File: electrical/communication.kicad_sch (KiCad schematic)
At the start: 13 parts

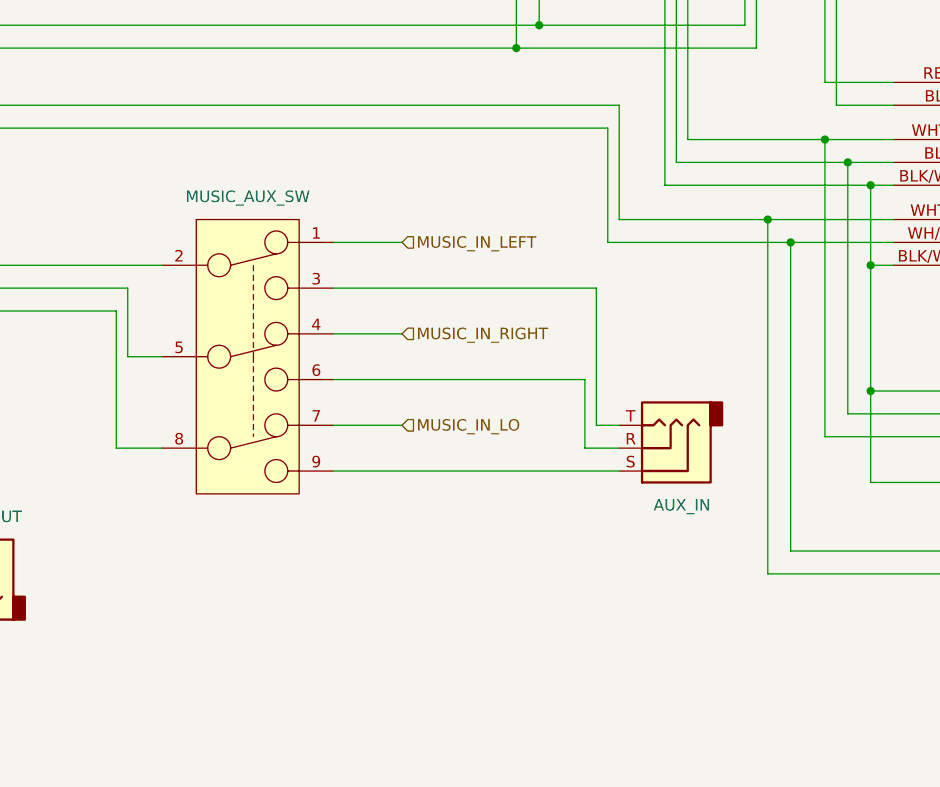
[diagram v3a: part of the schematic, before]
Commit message: Updated electrical to not use IBBS. Also, added BT adapter and 3P3T switch.
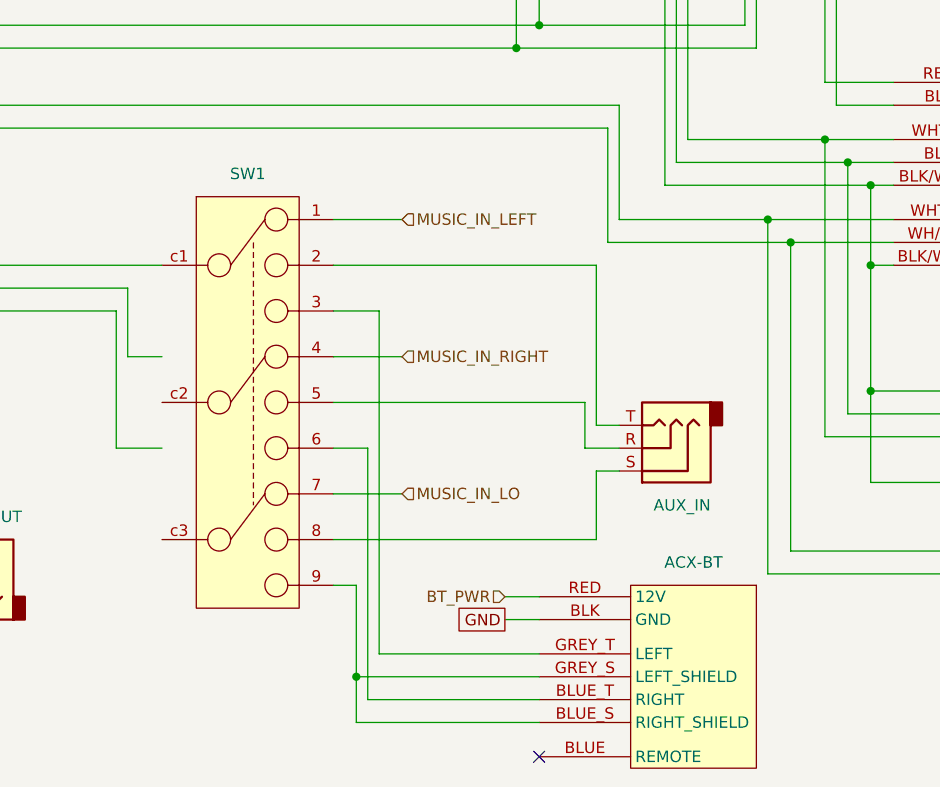
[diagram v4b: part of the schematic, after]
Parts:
- removed MUSIC_AUX_SW: ~, symbol flyerx:SW_3PDT_Toggle
- added ACX-BT: ~, symbol flyerx:AudioControl_ACX-BT1
- added SW1: ~, symbol flyerx:SW_3P3T
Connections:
- net GND: now also ACX-BT.BLK (GND)
- net MUSIC_IN_LEFT: now also SW1.1
- net MUSIC_IN_LO: now also SW1.7
- net MUSIC_IN_RIGHT: now also SW1.4
- net at AUX_IN.R: now also SW1.5
- net at AUX_IN.S: now also SW1.8
- net at AUX_IN.T: now also SW1.2
- net at GTR20.P2001_19 (MUSIC_IN_LEFT): now also SW1.c1
- new net: ACX-BT.GREY_T (LEFT), SW1.3
- new net: ACX-BT.BLUE_T (RIGHT), SW1.6
- new net: ACX-BT.BLUE_S (RIGHT_SHIELD), ACX-BT.GREY_S (LEFT_SHIELD), SW1.9
- new net BT_PWR: ACX-BT.RED (12V)
- no-connect marks 0 -> 1
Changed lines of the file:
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@@
   (junction (at 185.42 73.66) (diameter 0) (color 0 0 0 0)
   )
+  (junction (at 160.02 161.29) (diameter 0) (color 0 0 0 0)
+  )
   (junction (at 81.28 44.45) (diameter 0) (color 0 0 0 0)
   )
@@
   (junction (at 205.74 110.49) (diameter 0) (color 0 0 0 0)
   )
+  (no_connect (at 180.34 170.18))
   (wire (pts (xy 229.87 25.4) (xy 228.6 25.4))
     (stroke (width 0) (type default))
@@
     (stroke (width 0) (type default))
   )
+  (wire (pts (xy 176.53 152.4) (xy 180.34 152.4))
+    (stroke (width 0) (type default))
+  )
   (wire (pts (xy 106.68 124.46) (xy 106.68 151.13))
     (stroke (width 0) (type default))
@@
     (stroke (width 0) (type default))
   )
+  (wire (pts (xy 180.34 166.37) (xy 160.02 166.37))
+    (stroke (width 0) (type default))
+  )
   (wire (pts (xy 185.42 41.91) (xy 185.42 73.66))
     (stroke (width 0) (type default))
@@
     (stroke (width 0) (type default))
   )
-  (wire (pts (xy 157.48 118.11) (xy 186.69 118.11))
+  (wire (pts (xy 157.48 115.57) (xy 186.69 115.57))
     (stroke (width 0) (type default))
   )
@@
     (stroke (width 0) (type default))
   )
+  (wire (pts (xy 176.53 154.94) (xy 180.34 154.94))
+    (stroke (width 0) (type default))
+  )
   (wire (pts (xy 217.17 73.66) (xy 219.71 73.66))
     (stroke (width 0) (type default))
@@
     (stroke (width 0) (type default))
   )
+  (wire (pts (xy 161.29 135.89) (xy 157.48 135.89))
+    (stroke (width 0) (type default))
+  )
   (wire (pts (xy 73.66 80.01) (xy 195.58 80.01))
     (stroke (width 0) (type default))
@@
     (stroke (width 0) (type default))
   )
+  (wire (pts (xy 186.69 138.43) (xy 189.23 138.43))
+    (stroke (width 0) (type default))
+  )
   (wire (pts (xy 134.62 125.73) (xy 138.43 125.73))
     (stroke (width 0) (type default))
@@
     (stroke (width 0) (type default))
   )
+  (wire (pts (xy 160.02 161.29) (xy 160.02 151.13))
+    (stroke (width 0) (type default))
+  )
   (wire (pts (xy 204.47 80.01) (xy 219.71 80.01))
     (stroke (width 0) (type default))
@@
     (stroke (width 0) (type default))
   )
-  (wire (pts (xy 157.48 113.03) (xy 165.1 113.03))
+  (wire (pts (xy 186.69 146.05) (xy 186.69 138.43))
+    (stroke (width 0) (type default))
+  )
+  (wire (pts (xy 157.48 110.49) (xy 165.1 110.49))
     (stroke (width 0) (type default))
   )
@@
     (stroke (width 0) (type default))
   )
+  (wire (pts (xy 180.34 163.83) (xy 161.29 163.83))
+    (stroke (width 0) (type default))
+  )
   (wire (pts (xy 234.95 52.07) (xy 217.17 52.07))
     (stroke (width 0) (type default))
@@
     (stroke (width 0) (type default))
   )
+  (wire (pts (xy 160.02 161.29) (xy 160.02 166.37))
+    (stroke (width 0) (type default))
+  )
   (wire (pts (xy 73.66 73.66) (xy 185.42 73.66))
     (stroke (width 0) (type default))
@@
     (stroke (width 0) (type default))
   )
-  (wire (pts (xy 186.69 118.11) (xy 186.69 133.35))
+  (wire (pts (xy 186.69 115.57) (xy 186.69 133.35))
     (stroke (width 0) (type default))
   )
@@
     (stroke (width 0) (type default))
   )
-  (wire (pts (xy 157.48 123.19) (xy 165.1 123.19))
+  (wire (pts (xy 157.48 125.73) (xy 165.1 125.73))
     (stroke (width 0) (type default))
   )
@@
     (stroke (width 0) (type default))
   )
+  (wire (pts (xy 161.29 163.83) (xy 161.29 135.89))
+    (stroke (width 0) (type default))
+  )
   (wire (pts (xy 73.66 97.79) (xy 189.23 97.79))
     (stroke (width 0) (type default))
@@
     (stroke (width 0) (type default))
   )
-  (wire (pts (xy 185.42 128.27) (xy 185.42 135.89))
+  (wire (pts (xy 185.42 130.81) (xy 185.42 135.89))
     (stroke (width 0) (type default))
   )
@@
     (stroke (width 0) (type default))
   )
-  (wire (pts (xy 157.48 128.27) (xy 185.42 128.27))
+  (wire (pts (xy 160.02 161.29) (xy 180.34 161.29))
+    (stroke (width 0) (type default))
+  )
+  (wire (pts (xy 157.48 130.81) (xy 185.42 130.81))
     (stroke (width 0) (type default))
   )
@@
     (stroke (width 0) (type default))
   )
-  (wire (pts (xy 157.48 138.43) (xy 189.23 138.43))
+  (wire (pts (xy 157.48 146.05) (xy 186.69 146.05))
     (stroke (width 0) (type default))
   )
@@
     (stroke (width 0) (type default))
   )
-  (wire (pts (xy 157.48 133.35) (xy 165.1 133.35))
+  (wire (pts (xy 157.48 140.97) (xy 165.1 140.97))
     (stroke (width 0) (type default))
   )
@@
     (stroke (width 0) (type default))
   )
+  (wire (pts (xy 180.34 158.75) (xy 162.56 158.75))
+    (stroke (width 0) (type default))
+  )
   (wire (pts (xy 73.66 118.11) (xy 134.62 118.11))
     (stroke (width 0) (type default))
   )
+  (wire (pts (xy 162.56 158.75) (xy 162.56 120.65))
+    (stroke (width 0) (type default))
+  )
   (wire (pts (xy 73.66 77.47) (xy 196.85 77.47))
     (stroke (width 0) (type default))
@@
   )
   (wire (pts (xy 229.87 132.08) (xy 214.63 132.08))
+    (stroke (width 0) (type default))
+  )
+  (wire (pts (xy 162.56 120.65) (xy 157.48 120.65))
+    (stroke (width 0) (type default))
+  )
+  (wire (pts (xy 160.02 151.13) (xy 157.48 151.13))
     (stroke (width 0) (type default))
   )
@@
     (property "Intersheetrefs" "${INTERSHEET_REFS}" (at 60.3544 151.13 0)
       (effects (font (size 1.27 1.27)) (justify left) hide)
+    )
+  )
+  (global_label "GND" (shape passive) (at 176.53 154.94 180) (fields_autoplaced)
+    (effects (font (size 1.27 1.27)) (justify right))
+    (property "Intersheetrefs" "${INTERSHEET_REFS}" (at 170.7856 154.94 0)
+      (effects (font (size 1.27 1.27)) (justify right) hide)
     )
   )
@@
     (effects (font (size 1.27 1.27)) (justify left))
   )
-  (hierarchical_label "MUSIC_IN_LEFT" (shape input) (at 165.1 113.03 0) (fields_autoplaced)
+  (hierarchical_label "MUSIC_IN_LEFT" (shape input) (at 165.1 110.49 0) (fields_autoplaced)
     (effects (font (size 1.27 1.27)) (justify left))
   )
@@
     (effects (font (size 1.27 1.27)) (justify left))
   )
-  (hierarchical_label "MUSIC_IN_RIGHT" (shape input) (at 165.1 123.19 0) (fields_autoplaced)
-    (effects (font (size 1.27 1.27)) (justify left))
-  )
-  (hierarchical_label "MUSIC_IN_LO" (shape input) (at 165.1 133.35 0) (fields_autoplaced)
+  (hierarchical_label "MUSIC_IN_RIGHT" (shape input) (at 165.1 125.73 0) (fields_autoplaced)
+    (effects (font (size 1.27 1.27)) (justify left))
+  )
+  (hierarchical_label "MUSIC_IN_LO" (shape input) (at 165.1 140.97 0) (fields_autoplaced)
     (effects (font (size 1.27 1.27)) (justify left))
   )
   (hierarchical_label "CAN_HI_OUT" (shape output) (at 99.06 50.8 0) (fields_autoplaced)
     (effects (font (size 1.27 1.27)) (justify left))
+  )
+  (hierarchical_label "BT_PWR" (shape input) (at 176.53 152.4 180) (fields_autoplaced)
+    (effects (font (size 1.27 1.27)) (justify right))
   )
   (hierarchical_label "AUDIO_IN_HI" (shape input) (at 85.09 104.14 0) (fields_autoplaced)
@@
         (path "/e8ec215a-dbe2-4eba-a577-e50a0a128049/facdf550-4f2c-4387-974e-24c6900d900d"
           (reference "AUX_IN") (unit 1)
-        )
-      )
-    )
-  )
-  (symbol (lib_id "flyerx:SW_3PDT_Toggle") (at 148.59 110.49 0) (unit 1)
-    (in_bom yes) (on_board yes) (dnp no) (fields_autoplaced)
-    (property "Reference" "MUSIC_AUX_SW" (at 147.955 107.95 0)
-      (effects (font (size 1.27 1.27)))
-    )
-    (property "Value" "~" (at 142.24 110.49 0)
-      (effects (font (size 1.27 1.27)))
-    )
-    (property "Footprint" "" (at 142.24 110.49 0)
-      (effects (font (size 1.27 1.27)) hide)
-    )
-    (property "Datasheet" "" (at 142.24 110.49 0)
-      (effects (font (size 1.27 1.27)) hide)
-    )
-    (pin "3")
-    (pin "4")
-    (pin "1")
-    (pin "2")
-    (pin "7")
-    (pin "8")
-    (pin "9")
-    (pin "6")
-    (pin "5")
-    (instances
-      (project "electrical"
-        (path "/e8ec215a-dbe2-4eba-a577-e50a0a128049/facdf550-4f2c-4387-974e-24c6900d900d"
-          (reference "MUSIC_AUX_SW") (unit 1)
         )
       )
@@
         )
       )
+    )
+  )
+  (symbol (lib_id "flyerx:SW_3P3T") (at 148.59 107.95 0) (unit 1)
+    (in_bom yes) (on_board yes) (dnp no) (fields_autoplaced)
+    (property "Reference" "SW1" (at 147.955 105.41 0)
+      (effects (font (size 1.27 1.27)))
+    )
+    (property "Value" "~" (at 142.24 107.95 0)
+      (effects (font (size 1.27 1.27)))
+    )
+    (property "Footprint" "" (at 142.24 107.95 0)
+      (effects (font (size 1.27 1.27)) hide)
+    )
+    (property "Datasheet" "" (at 142.24 107.95 0)
+      (effects (font (size 1.27 1.27)) hide)
+    )
+    (pin "1")
+    (pin "2")
+    (pin "3")
+    (pin "4")
+    (pin "5")
+    (pin "6")
+    (pin "7")
+    (pin "8")
+    (pin "9")
+    (pin "c1")
+    (pin "c2")
+    (pin "c3")
+    (instances
+      (project "electrical"
+        (path "/e8ec215a-dbe2-4eba-a577-e50a0a128049/facdf550-4f2c-4387-974e-24c6900d900d"
+          (reference "SW1") (unit 1)
+        )
+      )
+    )
+  )
+  (symbol (lib_id "flyerx:AudioControl_ACX-BT1") (at 204.47 151.13 0) (mirror y) (unit 1)
+    (in_bom yes) (on_board yes) (dnp no)
+    (property "Reference" "ACX-BT" (at 197.485 148.59 0)
+      (effects (font (size 1.27 1.27)))
+    )
+    (property "Value" "~" (at 204.47 149.86 0)
+      (effects (font (size 1.27 1.27)))
+    )
+    (property "Footprint" "" (at 204.47 149.86 0)
+      (effects (font (size 1.27 1.27)) hide)
+    )
+    (property "Datasheet" "" (at 204.47 149.86 0)
+      (effects (font (size 1.27 1.27)) hide)
+    )
+    (pin "BLUE_S")
+    (pin "BLUE_T")
+    (pin "BLK")
+    (pin "BLUE")
+    (pin "RED")
+    (pin "GREY_S")
+    (pin "GREY_T")
+    (instances
+      (project "electrical"
+        (path "/e8ec215a-dbe2-4eba-a577-e50a0a128049/facdf550-4f2c-4387-974e-24c6900d900d"
+          (reference "ACX-BT") (unit 1)
+        )
+      )

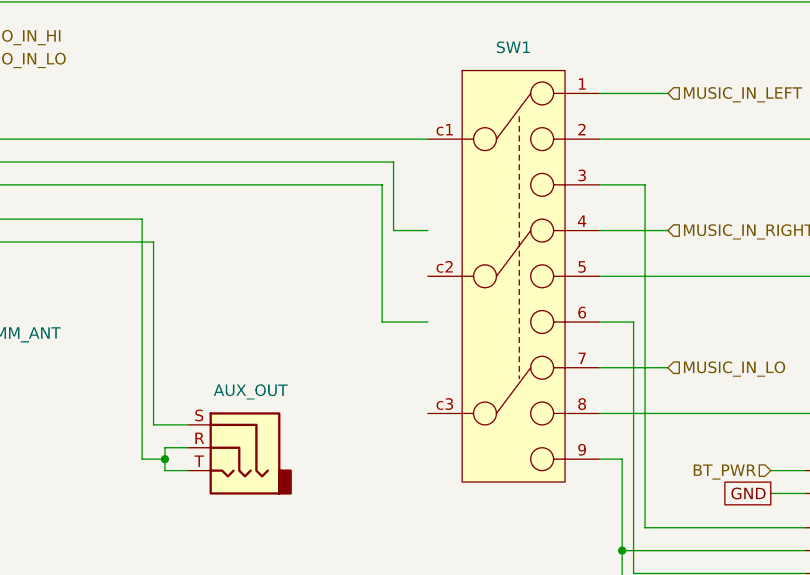
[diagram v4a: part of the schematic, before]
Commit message: Changed GTR CB to 7.5A. Added engine instrumentation. Added signal for fuel on.
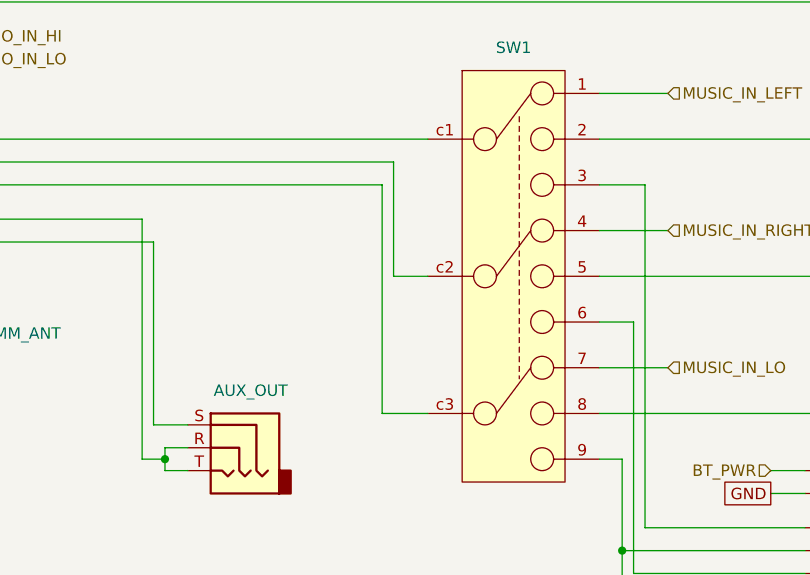
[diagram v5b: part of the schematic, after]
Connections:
- net at GTR20.P2001_18 (MUSIC_IN_RIGHT): now also SW1.c2
- net at GTR20.P2001_37 (MUSIC_LO): now also SW1.c3
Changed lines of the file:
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@@
   (title_block
     (title "Communication")
-    (date "2024-02-14")
-    (rev "0.9.3")
+    (date "2024-05-02")
+    (rev "0.9.4")
     (company "N877RV")
   )
@@
     (stroke (width 0) (type default))
   )
-  (wire (pts (xy 134.62 125.73) (xy 138.43 125.73))
+  (wire (pts (xy 134.62 130.81) (xy 138.43 130.81))
     (stroke (width 0) (type default))
   )
@@
     (stroke (width 0) (type default))
   )
-  (wire (pts (xy 133.35 135.89) (xy 138.43 135.89))
+  (wire (pts (xy 133.35 146.05) (xy 138.43 146.05))
     (stroke (width 0) (type default))
   )
@@
     (stroke (width 0) (type default))
   )
-  (wire (pts (xy 133.35 120.65) (xy 133.35 135.89))
+  (wire (pts (xy 133.35 120.65) (xy 133.35 146.05))
     (stroke (width 0) (type default))
   )
@@
     (stroke (width 0) (type default))
   )
-  (wire (pts (xy 134.62 118.11) (xy 134.62 125.73))
-    (stroke (width 0) (type default))
-  )
+  (wire (pts (xy 134.62 118.11) (xy 134.62 130.81))
+    (stroke (width 0) (type default))
+  )
